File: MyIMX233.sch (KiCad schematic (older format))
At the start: 81 parts, among them IC1 iMX233, IC2 DDR_SDRAM_MT46_x16, J1 USB_OTG, P1 P4v2, P2 1v2, P3 VDDA1v8, P4 2v5, P5 3v3, P6 P4v2, SW1 SWITCH_PUSHBUTTON, Y1 24Mhz

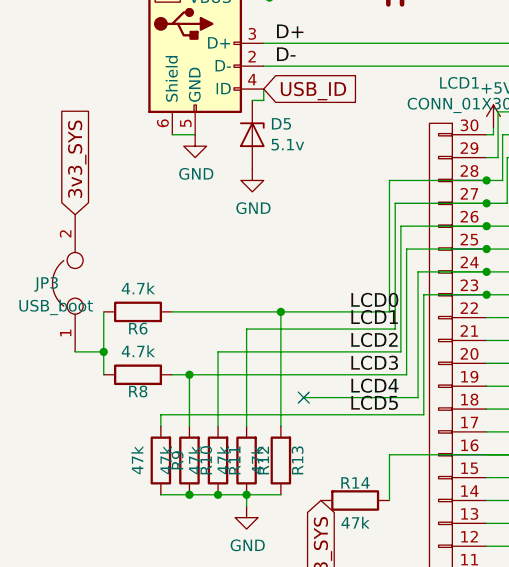
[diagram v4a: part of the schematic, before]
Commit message: boot resistors added
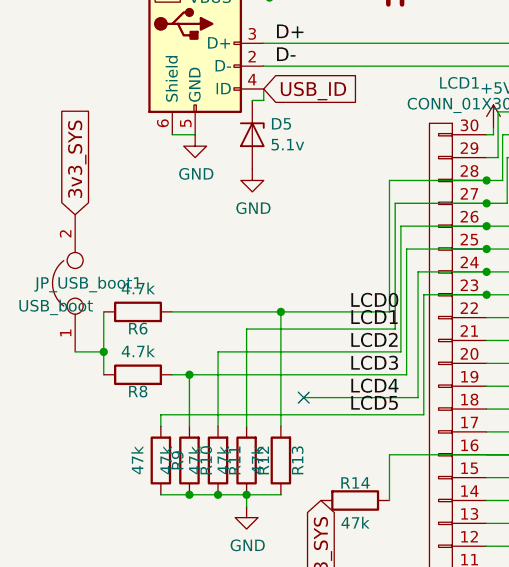
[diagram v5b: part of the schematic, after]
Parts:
- renumbered JP3 to JP_USB_boot1
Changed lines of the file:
@@
 $EndComp
 $Comp
-L +5V #PWR01
+L +5V #PWR22
 U 1 1 59061874
 P 5350 2500
-F 0 "#PWR01" H 5350 2350 50  0001 C CNN
+F 0 "#PWR22" H 5350 2350 50  0001 C CNN
 F 1 "+5V" H 5365 2673 50  0000 C CNN
 F 2 "" H 5350 2500 50  0001 C CNN
@@
 $EndComp
 $Comp
-L GND #PWR02
+L GND #PWR19
 U 1 1 59061CB5
 P 4350 1500
-F 0 "#PWR02" H 4350 1250 50  0001 C CNN
+F 0 "#PWR19" H 4350 1250 50  0001 C CNN
 F 1 "GND" H 4355 1327 50  0000 C CNN
 F 2 "" H 4350 1500 50  0001 C CNN
@@
 $EndComp
 $Comp
-L GND #PWR03
+L GND #PWR24
 U 1 1 59061F9B
 P 6500 1575
-F 0 "#PWR03" H 6500 1325 50  0001 C CNN
+F 0 "#PWR24" H 6500 1325 50  0001 C CNN
 F 1 "GND" H 6505 1402 50  0000 C CNN
 F 2 "" H 6500 1575 50  0001 C CNN
@@
 $EndComp
 $Comp
-L GND #PWR04
+L GND #PWR23
 U 1 1 59062213
 P 5900 1500
-F 0 "#PWR04" H 5900 1250 50  0001 C CNN
+F 0 "#PWR23" H 5900 1250 50  0001 C CNN
 F 1 "GND" H 5905 1327 50  0000 C CNN
 F 2 "" H 5900 1500 50  0001 C CNN
@@
 $EndComp
 $Comp
-L GND #PWR05
+L GND #PWR26
 U 1 1 590635F0
 P 7350 8900
-F 0 "#PWR05" H 7350 8650 50  0001 C CNN
+F 0 "#PWR26" H 7350 8650 50  0001 C CNN
 F 1 "GND" V 7355 8772 50  0000 R CNN
 F 2 "" H 7350 8900 50  0001 C CNN
@@
 VDAC_SYS
 $Comp
-L GND #PWR06
+L GND #PWR25
 U 1 1 59063BAA
 P 7350 8200
-F 0 "#PWR06" H 7350 7950 50  0001 C CNN
+F 0 "#PWR25" H 7350 7950 50  0001 C CNN
 F 1 "GND" V 7355 8072 50  0000 R CNN
 F 2 "" H 7350 8200 50  0001 C CNN
@@
 $EndComp
 $Comp
-L GND #PWR07
+L GND #PWR21
 U 1 1 59064432
 P 5200 9300
-F 0 "#PWR07" H 5200 9050 50  0001 C CNN
+F 0 "#PWR21" H 5200 9050 50  0001 C CNN
 F 1 "GND" H 5205 9127 50  0000 C CNN
 F 2 "" H 5200 9300 50  0001 C CNN
@@
 $EndComp
 $Comp
-L GND #PWR08
+L GND #PWR9
 U 1 1 590659AA
 P 1950 2800
-F 0 "#PWR08" H 1950 2550 50  0001 C CNN
+F 0 "#PWR9" H 1950 2550 50  0001 C CNN
 F 1 "GND" V 1955 2672 50  0000 R CNN
 F 2 "" H 1950 2800 50  0001 C CNN
@@
 $EndComp
 $Comp
-L GND #PWR09
+L GND #PWR28
 U 1 1 590668F6
 P 9800 6350
-F 0 "#PWR09" H 9800 6100 50  0001 C CNN
+F 0 "#PWR28" H 9800 6100 50  0001 C CNN
 F 1 "GND" H 9805 6177 50  0000 C CNN
 F 2 "" H 9800 6350 50  0001 C CNN
@@
 $EndComp
 $Comp
-L GND #PWR010
+L GND #PWR29
 U 1 1 59069F3D
 P 10300 2050
-F 0 "#PWR010" H 10300 1800 50  0001 C CNN
+F 0 "#PWR29" H 10300 1800 50  0001 C CNN
 F 1 "GND" H 10305 1877 50  0000 C CNN
 F 2 "" H 10300 2050 50  0001 C CNN
@@
 $EndComp
 $Comp
-L GND #PWR011
+L GND #PWR27
 U 1 1 5906A1D6
 P 9250 2100
-F 0 "#PWR011" H 9250 1850 50  0001 C CNN
+F 0 "#PWR27" H 9250 1850 50  0001 C CNN
 F 1 "GND" H 9255 1927 50  0000 C CNN
 F 2 "" H 9250 2100 50  0001 C CNN
@@
 $EndComp
 $Comp
-L +5V #PWR012
+L +5V #PWR8
 U 1 1 5906AB53
 P 1650 3250
-F 0 "#PWR012" H 1650 3100 50  0001 C CNN
+F 0 "#PWR8" H 1650 3100 50  0001 C CNN
 F 1 "+5V" H 1665 3423 50  0000 C CNN
 F 2 "" H 1650 3250 50  0001 C CNN
@@
 $EndComp
 $Comp
-L GND #PWR013
+L GND #PWR3
 U 1 1 5906AC36
 P 1225 3900
-F 0 "#PWR013" H 1225 3650 50  0001 C CNN
+F 0 "#PWR3" H 1225 3650 50  0001 C CNN
 F 1 "GND" H 1230 3727 50  0000 C CNN
 F 2 "" H 1225 3900 50  0001 C CNN
@@
 $EndComp
 $Comp
-L GND #PWR014
+L GND #PWR15
 U 1 1 5907F39E
 P 2750 7000
-F 0 "#PWR014" H 2750 6750 50  0001 C CNN
+F 0 "#PWR15" H 2750 6750 50  0001 C CNN
 F 1 "GND" H 2755 6827 50  0000 C CNN
 F 2 "" H 2750 7000 50  0001 C CNN
@@
 $EndComp
 $Comp
-L GND #PWR015
+L GND #PWR14
 U 1 1 59081628
 P 2650 7550
-F 0 "#PWR015" H 2650 7300 50  0001 C CNN
+F 0 "#PWR14" H 2650 7300 50  0001 C CNN
 F 1 "GND" H 2655 7377 50  0000 C CNN
 F 2 "" H 2650 7550 50  0001 C CNN
@@
 $EndComp
 $Comp
-L GND #PWR016
+L GND #PWR7
 U 1 1 590823FE
 P 1600 9350
-F 0 "#PWR016" H 1600 9100 50  0001 C CNN
+F 0 "#PWR7" H 1600 9100 50  0001 C CNN
 F 1 "GND" V 1605 9222 50  0000 R CNN
 F 2 "" H 1600 9350 50  0001 C CNN
@@
 NoConn ~ 3250 5800
 $Comp
-L GND #PWR017
+L GND #PWR13
 U 1 1 59087C8C
 P 2650 5600
-F 0 "#PWR017" H 2650 5350 50  0001 C CNN
+F 0 "#PWR13" H 2650 5350 50  0001 C CNN
 F 1 "GND" V 2655 5472 50  0000 R CNN
 F 2 "" H 2650 5600 50  0001 C CNN
@@
 $EndComp
 $Comp
-L +5V #PWR018
+L +5V #PWR11
 U 1 1 5908D2ED
 P 2530 3870
-F 0 "#PWR018" H 2530 3720 50  0001 C CNN
+F 0 "#PWR11" H 2530 3720 50  0001 C CNN
 F 1 "+5V" H 2545 4043 50  0000 C CNN
 F 2 "" H 2530 3870 50  0001 C CNN
@@
 $EndComp
 $Comp
-L GND #PWR019
+L GND #PWR17
 U 1 1 59093EF0
 P 3200 9900
-F 0 "#PWR019" H 3200 9650 50  0001 C CNN
+F 0 "#PWR17" H 3200 9650 50  0001 C CNN
 F 1 "GND" H 3205 9727 50  0000 C CNN
 F 2 "" H 3200 9900 50  0001 C CNN
@@
 $EndComp
 $Comp
-L GND #PWR020
+L GND #PWR10
 U 1 1 5907493E
 P 2350 2300
-F 0 "#PWR020" H 2350 2050 50  0001 C CNN
+F 0 "#PWR10" H 2350 2050 50  0001 C CNN
 F 1 "GND" V 2355 2172 50  0000 R CNN
 F 2 "" H 2350 2300 50  0001 C CNN
@@
 $EndComp
 $Comp
-L GND #PWR021
+L GND #PWR20
 U 1 1 592FC254
 P 4625 525
-F 0 "#PWR021" H 4625 275 50  0001 C CNN
+F 0 "#PWR20" H 4625 275 50  0001 C CNN
 F 1 "GND" H 4630 352 50  0000 C CNN
 F 2 "" H 4625 525 50  0001 C CNN
@@
 $EndComp
 $Comp
-L GND #PWR022
+L GND #PWR18
 U 1 1 592FDAC8
 P 3575 1050
-F 0 "#PWR022" H 3575 800 50  0001 C CNN
+F 0 "#PWR18" H 3575 800 50  0001 C CNN
 F 1 "GND" H 3580 877 50  0000 C CNN
 F 2 "" H 3575 1050 50  0001 C CNN
@@
 $EndComp
 $Comp
-L GND #PWR023
+L GND #PWR16
 U 1 1 59330AE2
 P 3075 2775
-F 0 "#PWR023" H 3075 2525 50  0001 C CNN
+F 0 "#PWR16" H 3075 2525 50  0001 C CNN
 F 1 "GND" H 3080 2602 50  0000 C CNN
 F 2 "" H 3075 2775 50  0001 C CNN
@@
 $EndComp
 $Comp
-L GND #PWR024
+L GND #PWR4
 U 1 1 593BA16F
 P 1275 7475
-F 0 "#PWR024" H 1275 7225 50  0001 C CNN
+F 0 "#PWR4" H 1275 7225 50  0001 C CNN
 F 1 "GND" H 1280 7302 50  0000 C CNN
 F 2 "" H 1275 7475 50  0001 C CNN
@@
 $EndComp
 $Comp
-L +5V #PWR025
+L +5V #PWR12
 U 1 1 593CE4C1
 P 2600 7925
-F 0 "#PWR025" H 2600 7775 50  0001 C CNN
+F 0 "#PWR12" H 2600 7775 50  0001 C CNN
 F 1 "+5V" H 2615 8098 50  0000 C CNN
 F 2 "" H 2600 7925 50  0001 C CNN
@@
 $EndComp
 $Comp
-L +5V #PWR026
+L +5V #PWR1
 U 1 1 598B5CE8
 P 750 2650
-F 0 "#PWR026" H 750 2500 50  0001 C CNN
+F 0 "#PWR1" H 750 2500 50  0001 C CNN
 F 1 "+5V" H 765 2823 50  0000 C CNN
 F 2 "" H 750 2650 50  0001 C CNN
@@
 $EndComp
 $Comp
-L GND #PWR027
+L GND #PWR2
 U 1 1 598B5D7D
 P 750 3100
-F 0 "#PWR027" H 750 2850 50  0001 C CNN
+F 0 "#PWR2" H 750 2850 50  0001 C CNN
 F 1 "GND" H 755 2927 50  0000 C CNN
 F 2 "" H 750 3100 50  0001 C CNN
@@
 $EndComp
 $Comp
-L GND #PWR028
+L GND #PWR6
 U 1 1 598BC5E8
 P 1475 4050
-F 0 "#PWR028" H 1475 3800 50  0001 C CNN
+F 0 "#PWR6" H 1475 3800 50  0001 C CNN
 F 1 "GND" H 1480 3877 50  0000 C CNN
 F 2 "" H 1475 4050 50  0001 C CNN
@@
 $EndComp
 $Comp
-L GND #PWR029
+L GND #PWR5
 U 1 1 599401F2
 P 1450 5525
-F 0 "#PWR029" H 1450 5275 50  0001 C CNN
+F 0 "#PWR5" H 1450 5275 50  0001 C CNN
 F 1 "GND" H 1455 5352 50  0000 C CNN
 F 2 "" H 1450 5525 50  0001 C CNN
@@
 3v3_SYS
 $Comp
-L Jumper JP3
+L Jumper JP_USB_boot1
 U 1 1 59949205
 P 700 4550
-F 0 "JP3" V 700 4725 50  0000 R CNN
+F 0 "JP_USB_boot1" V 700 4725 50  0000 R CNN
 F 1 "USB_boot" V 600 4800 50  0000 R CNN
 F 2 "Pin_Headers:Pin_Header_Straight_1x02_Pitch2.54mm" H 700 4550 50  0001 C CNN

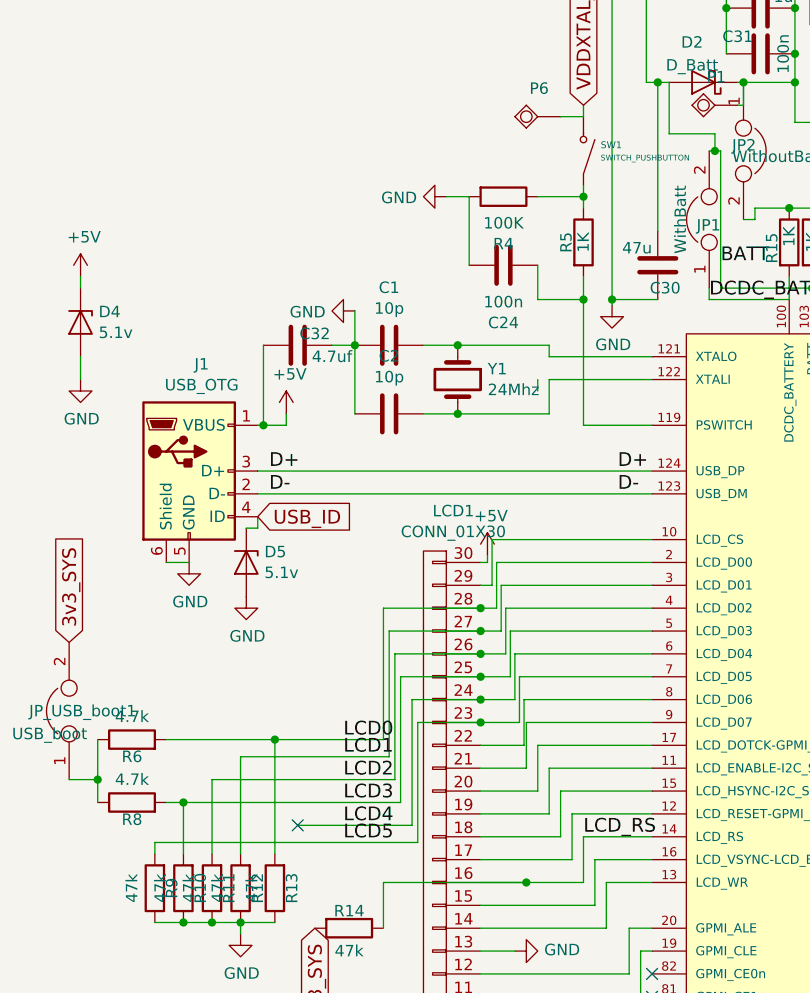
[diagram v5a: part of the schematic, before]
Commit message: re routed because of pad length extention to 2mm. Generated gerver files too
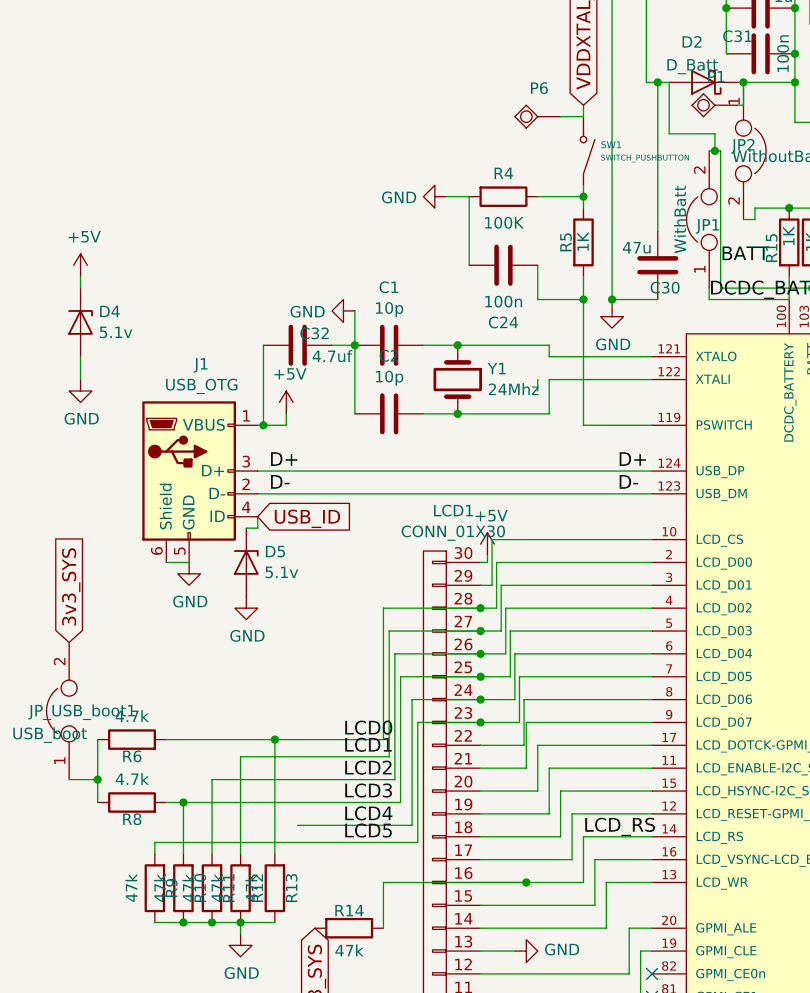
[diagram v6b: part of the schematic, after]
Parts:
- IC1: footprint Housings_QFP:LQFP-128_14x14mm_Pitch0.4mm -> mylib:LQFP-128_14x14mm_Pitch0.4mm
- P1: value P4v2 -> 4p2
- P6: value P4v2 -> 1v
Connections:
- no-connect marks 20 -> 19
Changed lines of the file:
@@
 F 0 "IC1" H 5000 2656 60  0000 C CNN
 F 1 "iMX233" H 5000 2550 60  0000 C CNN
-F 2 "Housings_QFP:LQFP-128_14x14mm_Pitch0.4mm" H 5000 5900 60  0001 C CNN
+F 2 "mylib:LQFP-128_14x14mm_Pitch0.4mm" H 5000 5900 60  0001 C CNN
 F 3 "" H 5000 5900 60  0001 C CNN
 	1    5000 5900
@@
 $EndComp
 $Comp
-L +5V #PWR22
+L +5V #PWR01
 U 1 1 59061874
 P 5350 2500
-F 0 "#PWR22" H 5350 2350 50  0001 C CNN
+F 0 "#PWR01" H 5350 2350 50  0001 C CNN
 F 1 "+5V" H 5365 2673 50  0000 C CNN
 F 2 "" H 5350 2500 50  0001 C CNN
@@
 $EndComp
 $Comp
-L GND #PWR19
+L GND #PWR02
 U 1 1 59061CB5
 P 4350 1500
-F 0 "#PWR19" H 4350 1250 50  0001 C CNN
+F 0 "#PWR02" H 4350 1250 50  0001 C CNN
 F 1 "GND" H 4355 1327 50  0000 C CNN
 F 2 "" H 4350 1500 50  0001 C CNN
@@
 $EndComp
 $Comp
-L GND #PWR24
+L GND #PWR03
 U 1 1 59061F9B
 P 6500 1575
-F 0 "#PWR24" H 6500 1325 50  0001 C CNN
+F 0 "#PWR03" H 6500 1325 50  0001 C CNN
 F 1 "GND" H 6505 1402 50  0000 C CNN
 F 2 "" H 6500 1575 50  0001 C CNN
@@
 $EndComp
 $Comp
-L GND #PWR23
+L GND #PWR04
 U 1 1 59062213
 P 5900 1500
-F 0 "#PWR23" H 5900 1250 50  0001 C CNN
+F 0 "#PWR04" H 5900 1250 50  0001 C CNN
 F 1 "GND" H 5905 1327 50  0000 C CNN
 F 2 "" H 5900 1500 50  0001 C CNN
@@
 $EndComp
 $Comp
-L GND #PWR26
+L GND #PWR05
 U 1 1 590635F0
 P 7350 8900
-F 0 "#PWR26" H 7350 8650 50  0001 C CNN
+F 0 "#PWR05" H 7350 8650 50  0001 C CNN
 F 1 "GND" V 7355 8772 50  0000 R CNN
 F 2 "" H 7350 8900 50  0001 C CNN
@@
 VDAC_SYS
 $Comp
-L GND #PWR25
+L GND #PWR06
 U 1 1 59063BAA
 P 7350 8200
-F 0 "#PWR25" H 7350 7950 50  0001 C CNN
+F 0 "#PWR06" H 7350 7950 50  0001 C CNN
 F 1 "GND" V 7355 8072 50  0000 R CNN
 F 2 "" H 7350 8200 50  0001 C CNN
@@
 $EndComp
 $Comp
-L GND #PWR21
+L GND #PWR07
 U 1 1 59064432
 P 5200 9300
-F 0 "#PWR21" H 5200 9050 50  0001 C CNN
+F 0 "#PWR07" H 5200 9050 50  0001 C CNN
 F 1 "GND" H 5205 9127 50  0000 C CNN
 F 2 "" H 5200 9300 50  0001 C CNN
@@
 $EndComp
 $Comp
-L GND #PWR9
+L GND #PWR08
 U 1 1 590659AA
 P 1950 2800
-F 0 "#PWR9" H 1950 2550 50  0001 C CNN
+F 0 "#PWR08" H 1950 2550 50  0001 C CNN
 F 1 "GND" V 1955 2672 50  0000 R CNN
 F 2 "" H 1950 2800 50  0001 C CNN
@@
 $EndComp
 $Comp
-L GND #PWR28
+L GND #PWR09
 U 1 1 590668F6
 P 9800 6350
-F 0 "#PWR28" H 9800 6100 50  0001 C CNN
+F 0 "#PWR09" H 9800 6100 50  0001 C CNN
 F 1 "GND" H 9805 6177 50  0000 C CNN
 F 2 "" H 9800 6350 50  0001 C CNN
@@
 $EndComp
 $Comp
-L GND #PWR29
+L GND #PWR010
 U 1 1 59069F3D
 P 10300 2050
-F 0 "#PWR29" H 10300 1800 50  0001 C CNN
+F 0 "#PWR010" H 10300 1800 50  0001 C CNN
 F 1 "GND" H 10305 1877 50  0000 C CNN
 F 2 "" H 10300 2050 50  0001 C CNN
@@
 $EndComp
 $Comp
-L GND #PWR27
+L GND #PWR011
 U 1 1 5906A1D6
 P 9250 2100
-F 0 "#PWR27" H 9250 1850 50  0001 C CNN
+F 0 "#PWR011" H 9250 1850 50  0001 C CNN
 F 1 "GND" H 9255 1927 50  0000 C CNN
 F 2 "" H 9250 2100 50  0001 C CNN
@@
 $EndComp
 $Comp
-L +5V #PWR8
+L +5V #PWR012
 U 1 1 5906AB53
 P 1650 3250
-F 0 "#PWR8" H 1650 3100 50  0001 C CNN
+F 0 "#PWR012" H 1650 3100 50  0001 C CNN
 F 1 "+5V" H 1665 3423 50  0000 C CNN
 F 2 "" H 1650 3250 50  0001 C CNN
@@
 $EndComp
 $Comp
-L GND #PWR3
+L GND #PWR013
 U 1 1 5906AC36
 P 1225 3900
-F 0 "#PWR3" H 1225 3650 50  0001 C CNN
+F 0 "#PWR013" H 1225 3650 50  0001 C CNN
 F 1 "GND" H 1230 3727 50  0000 C CNN
 F 2 "" H 1225 3900 50  0001 C CNN
@@
 $EndComp
 $Comp
-L GND #PWR15
+L GND #PWR014
 U 1 1 5907F39E
 P 2750 7000
-F 0 "#PWR15" H 2750 6750 50  0001 C CNN
+F 0 "#PWR014" H 2750 6750 50  0001 C CNN
 F 1 "GND" H 2755 6827 50  0000 C CNN
 F 2 "" H 2750 7000 50  0001 C CNN
@@
 $EndComp
 $Comp
-L GND #PWR14
+L GND #PWR015
 U 1 1 59081628
 P 2650 7550
-F 0 "#PWR14" H 2650 7300 50  0001 C CNN
+F 0 "#PWR015" H 2650 7300 50  0001 C CNN
 F 1 "GND" H 2655 7377 50  0000 C CNN
 F 2 "" H 2650 7550 50  0001 C CNN
@@
 $EndComp
 $Comp
-L GND #PWR7
+L GND #PWR016
 U 1 1 590823FE
 P 1600 9350
-F 0 "#PWR7" H 1600 9100 50  0001 C CNN
+F 0 "#PWR016" H 1600 9100 50  0001 C CNN
 F 1 "GND" V 1605 9222 50  0000 R CNN
 F 2 "" H 1600 9350 50  0001 C CNN
@@
 NoConn ~ 3250 5800
 $Comp
-L GND #PWR13
+L GND #PWR017
 U 1 1 59087C8C
 P 2650 5600
-F 0 "#PWR13" H 2650 5350 50  0001 C CNN
+F 0 "#PWR017" H 2650 5350 50  0001 C CNN
 F 1 "GND" V 2655 5472 50  0000 R CNN
 F 2 "" H 2650 5600 50  0001 C CNN
@@
 $EndComp
 $Comp
-L +5V #PWR11
+L +5V #PWR018
 U 1 1 5908D2ED
 P 2530 3870
-F 0 "#PWR11" H 2530 3720 50  0001 C CNN
+F 0 "#PWR018" H 2530 3720 50  0001 C CNN
 F 1 "+5V" H 2545 4043 50  0000 C CNN
 F 2 "" H 2530 3870 50  0001 C CNN
@@
 $EndComp
 $Comp
-L GND #PWR17
+L GND #PWR019
 U 1 1 59093EF0
 P 3200 9900
-F 0 "#PWR17" H 3200 9650 50  0001 C CNN
+F 0 "#PWR019" H 3200 9650 50  0001 C CNN
 F 1 "GND" H 3205 9727 50  0000 C CNN
 F 2 "" H 3200 9900 50  0001 C CNN
@@
 U 1 1 59074059
 P 2600 2300
-F 0 "R4" V 2807 2300 50  0000 C CNN
+F 0 "R4" V 2500 2300 50  0000 C CNN
 F 1 "100K" V 2716 2300 50  0000 C CNN
 F 2 "Resistors_SMD:R_0603_HandSoldering" V 2530 2300 50  0001 C CNN
@@
 $EndComp
 $Comp
-L GND #PWR10
+L GND #PWR020
 U 1 1 5907493E
 P 2350 2300
-F 0 "#PWR10" H 2350 2050 50  0001 C CNN
+F 0 "#PWR020" H 2350 2050 50  0001 C CNN
 F 1 "GND" V 2355 2172 50  0000 R CNN
 F 2 "" H 2350 2300 50  0001 C CNN
@@
 $EndComp
 $Comp
-L GND #PWR20
+L GND #PWR021
 U 1 1 592FC254
 P 4625 525
-F 0 "#PWR20" H 4625 275 50  0001 C CNN
+F 0 "#PWR021" H 4625 275 50  0001 C CNN
 F 1 "GND" H 4630 352 50  0000 C CNN
 F 2 "" H 4625 525 50  0001 C CNN
@@
 $EndComp
 $Comp
-L GND #PWR18
+L GND #PWR022
 U 1 1 592FDAC8
 P 3575 1050
-F 0 "#PWR18" H 3575 800 50  0001 C CNN
+F 0 "#PWR022" H 3575 800 50  0001 C CNN
 F 1 "GND" H 3580 877 50  0000 C CNN
 F 2 "" H 3575 1050 50  0001 C CNN
@@
 P 3525 1900
 F 0 "P1" V 3402 1906 50  0000 C CNN
-F 1 "P4v2" H 3525 1900 50  0001 L BNN
+F 1 "4p2" H 3525 1900 50  0001 L BNN
 F 2 "iMX233-OLinuXino-NANO_Rev_BEagle:GOGO_TESTPAD2" H 3555 2050 20  0001 C CNN
 F 3 "" H 3525 1900 60  0001 C CNN
@@
 $EndComp
 $Comp
-L GND #PWR16
+L GND #PWR023
 U 1 1 59330AE2
 P 3075 2775
-F 0 "#PWR16" H 3075 2525 50  0001 C CNN
+F 0 "#PWR023" H 3075 2525 50  0001 C CNN
 F 1 "GND" H 3080 2602 50  0000 C CNN
 F 2 "" H 3075 2775 50  0001 C CNN
@@
 $EndComp
 $Comp
-L GND #PWR4
+L GND #PWR024
 U 1 1 593BA16F
 P 1275 7475
-F 0 "#PWR4" H 1275 7225 50  0001 C CNN
+F 0 "#PWR024" H 1275 7225 50  0001 C CNN
 F 1 "GND" H 1280 7302 50  0000 C CNN
 F 2 "" H 1275 7475 50  0001 C CNN
@@
 $EndComp
 $Comp
-L +5V #PWR12
+L +5V #PWR025
 U 1 1 593CE4C1
 P 2600 7925
-F 0 "#PWR12" H 2600 7775 50  0001 C CNN
+F 0 "#PWR025" H 2600 7775 50  0001 C CNN
 F 1 "+5V" H 2615 8098 50  0000 C CNN
 F 2 "" H 2600 7925 50  0001 C CNN
@@
 $EndComp
 $Comp
-L +5V #PWR1
+L +5V #PWR026
 U 1 1 598B5CE8
 P 750 2650
-F 0 "#PWR1" H 750 2500 50  0001 C CNN
+F 0 "#PWR026" H 750 2500 50  0001 C CNN
 F 1 "+5V" H 765 2823 50  0000 C CNN
 F 2 "" H 750 2650 50  0001 C CNN
@@
 $EndComp
 $Comp
-L GND #PWR2
+L GND #PWR027
 U 1 1 598B5D7D
 P 750 3100
-F 0 "#PWR2" H 750 2850 50  0001 C CNN
+F 0 "#PWR027" H 750 2850 50  0001 C CNN
 F 1 "GND" H 755 2927 50  0000 C CNN
 F 2 "" H 750 3100 50  0001 C CNN
@@
 $EndComp
 $Comp
-L GND #PWR6
+L GND #PWR028
 U 1 1 598BC5E8
 P 1475 4050
-F 0 "#PWR6" H 1475 3800 50  0001 C CNN
+F 0 "#PWR028" H 1475 3800 50  0001 C CNN
 F 1 "GND" H 1480 3877 50  0000 C CNN
 F 2 "" H 1475 4050 50  0001 C CNN
@@
 P 2750 1950
 F 0 "P6" V 2627 1956 50  0000 C CNN
-F 1 "P4v2" H 2750 1950 50  0001 L BNN
+F 1 "1v" H 2750 1950 50  0001 L BNN
 F 2 "iMX233-OLinuXino-NANO_Rev_BEagle:GOGO_TESTPAD2" H 2780 2100 20  0001 C CNN
 F 3 "" H 2750 1950 60  0001 C CNN
@@
 $EndComp
 $Comp
-L GND #PWR5
+L GND #PWR029
 U 1 1 599401F2
 P 1450 5525
-F 0 "#PWR5" H 1450 5275 50  0001 C CNN
+F 0 "#PWR029" H 1450 5275 50  0001 C CNN
 F 1 "GND" H 1455 5352 50  0000 C CNN
 F 2 "" H 1450 5525 50  0001 C CNN
@@
 	-1   0    0    1
 $EndComp
-NoConn ~ 1700 5050
 $Comp
 L R R9
